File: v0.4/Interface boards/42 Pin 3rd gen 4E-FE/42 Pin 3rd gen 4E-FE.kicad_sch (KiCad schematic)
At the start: 11 parts, among them J1 4E-FE OEM, J2 KNOCK, J3 Speeduino, J4 Conn_02x20_Counter_Clockwise, J5 Conn_01x02, J6 STARTER

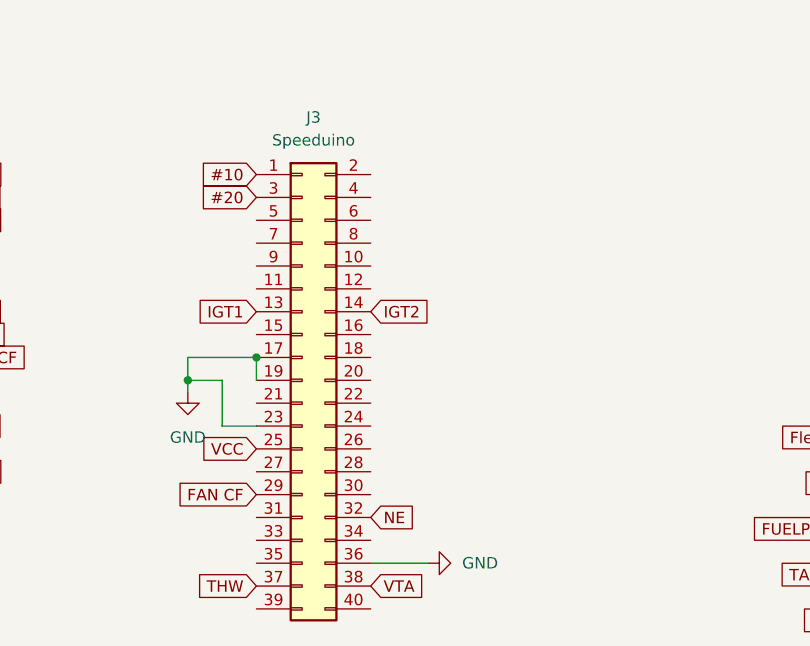
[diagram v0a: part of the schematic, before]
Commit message: Updated Interface board to include VR pickup negative side. Added ground plane to top side.
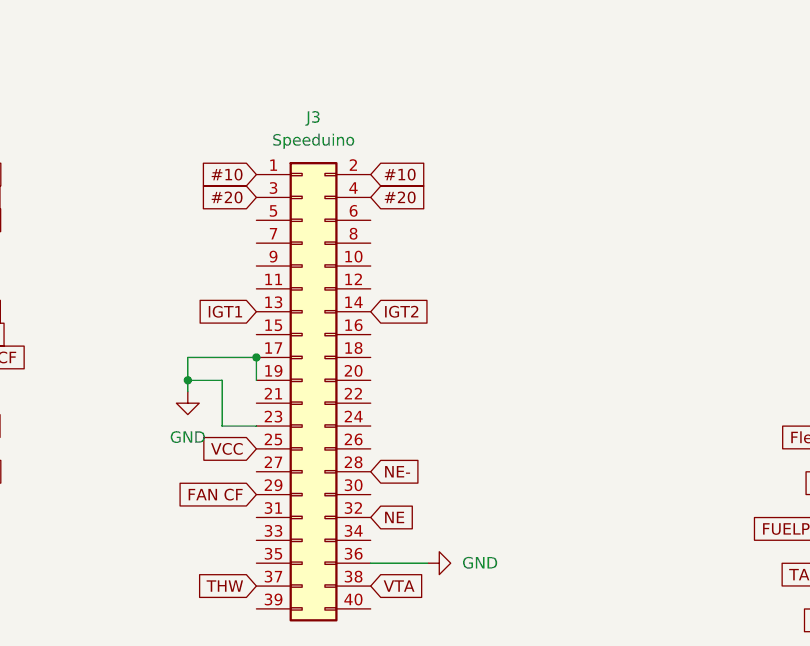
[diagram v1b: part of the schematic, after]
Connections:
- net #10: now also J3.2 (Pin_2)
- net #20: now also J3.4 (Pin_4)
- net NE-: now also J3.28 (Pin_28)
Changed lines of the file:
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@@
+		)
+	)
+	(global_label "#10"
+		(shape input)
+		(at 135.89 72.39 0)
+		(fields_autoplaced yes)
+		(effects
+			(font
+				(size 1.27 1.27)
+			)
+			(justify left)
+		)
+		(property "Intersheetrefs" "${INTERSHEET_REFS}"
+			(at 142.5642 72.39 0)
+			(effects
+				(font
+					(size 1.27 1.27)
+				)
+				(justify left)
+				(hide yes)
+			)
 		)
 	)
@@
 		)
 	)
+	(global_label "#20"
+		(shape input)
+		(at 135.89 74.93 0)
+		(fields_autoplaced yes)
+		(effects
+			(font
+				(size 1.27 1.27)
+			)
+			(justify left)
+		)
+		(property "Intersheetrefs" "${INTERSHEET_REFS}"
+			(at 142.5642 74.93 0)
+			(effects
+				(font
+					(size 1.27 1.27)
+				)
+				(justify left)
+				(hide yes)
+			)
+		)
+	)
 	(global_label "IGN-4-OUT"
 		(shape input)
@@
 				(hide yes)
 			)
+		)
+	)
+	(global_label "NE-"
+		(shape input)
+		(at 135.89 105.41 0)
+		(fields_autoplaced yes)
+		(effects
+			(font
+				(size 1.27 1.27)
+			)
+			(justify left)
+		)
+		(property "Intersheetrefs" "${INTERSHEET_REFS}"
+			(at 142.9271 105.41 0)
+			(effects
+				(font
+					(size 1.27 1.27)
+				)
+				(justify left)
+				(hide yes)
+			)
